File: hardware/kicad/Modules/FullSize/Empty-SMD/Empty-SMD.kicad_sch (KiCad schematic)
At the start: 5 parts, among them J1 Conn_02x07_Odd_Even, U1 24AA025E-OT

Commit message: Fix EEPROM values and DuoRelay R5 footprint
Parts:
- U1: value 24AA025E-OT -> 24AA025E64T-I/OT
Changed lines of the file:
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@@
 			)
 		)
-		(property "Value" "24AA025E-OT"
+		(property "Value" "24AA025E64T-I/OT"
 			(at 185.0233 72.39 0)
 			(show_name no)

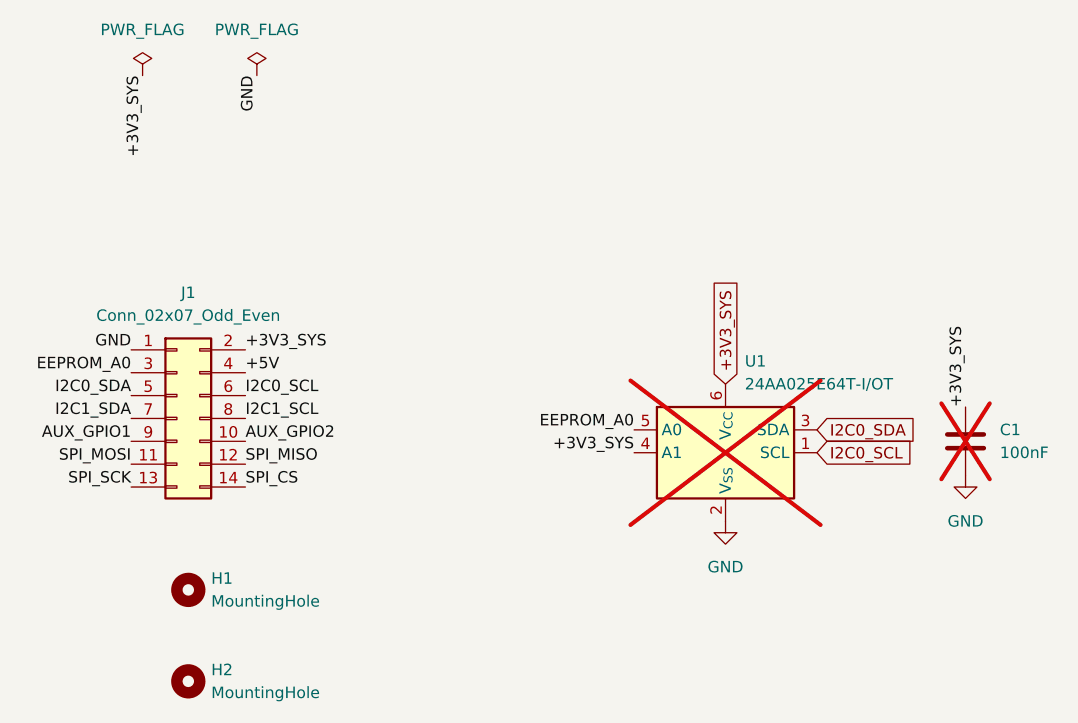
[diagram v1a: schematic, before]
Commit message: Complete Rev 0.3 module schematics
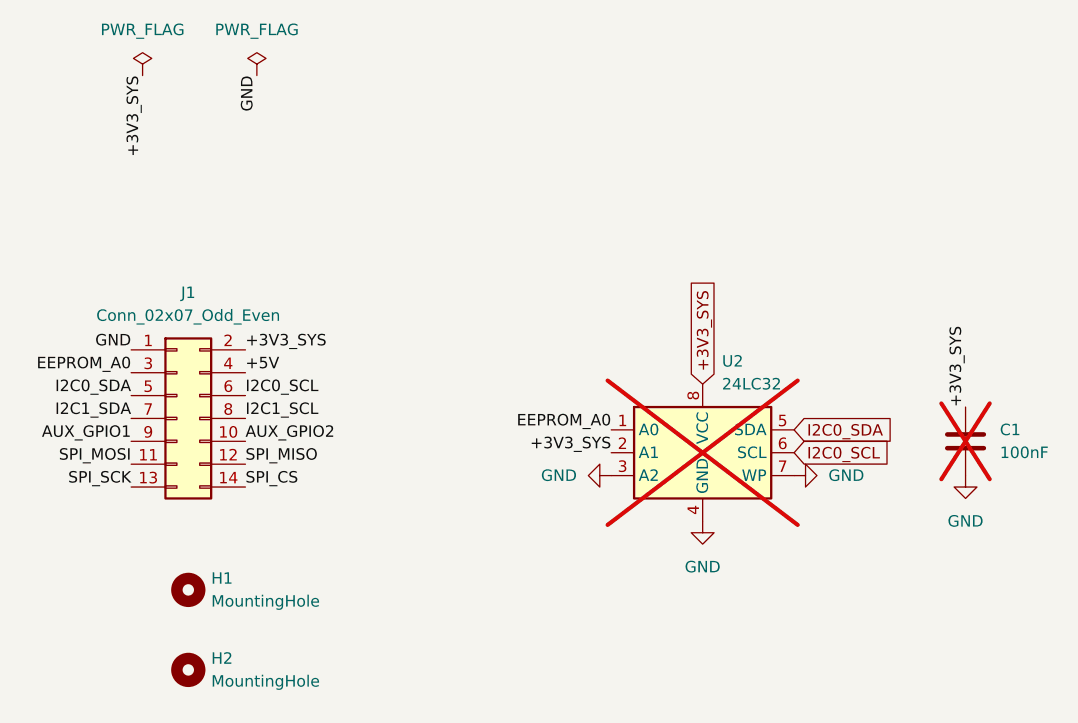
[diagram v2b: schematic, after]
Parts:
- removed U1: 24AA025E64T-I/OT, Package_TO_SOT_SMD:SOT-23-6, symbol Memory_EEPROM:24AA025E-OT
- added U2: 24LC32, Package_SO:SOIC-8_3.9x4.9mm_P1.27mm, symbol Memory_EEPROM:24LC32
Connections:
- net +3V3_SYS: now also U2.2 (A1), U2.8 (VCC)
- net EEPROM_A0: now also U2.1 (A0)
- net GND: now also U2.3 (A2), U2.4 (GND), U2.7 (WP)
- net I2C0_SCL: now also U2.6 (SCL)
- net I2C0_SDA: now also U2.5 (SDA)
